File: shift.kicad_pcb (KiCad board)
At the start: 2 copper layers, 24 parts, among them P1 5v, P2 5v, P3 15Vpower-fixme, P4 digiin, P5 digicascade, P6 analog, P7 analog, P8 out, U1 74HC595, U2 TL074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

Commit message: updates... added correct header
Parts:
- added C5: 100n, Capacitors_ThroughHole:C_Rect_L7_W4.5_P5, F.Cu at (26.7, 50.5)
- added C6: 10uF, Discret:CP20, F.Cu at (110.2, 43.9)
- added C7: 10uF, Discret:CP20, F.Cu at (109.7, 71.6)
- added C8: 100n, Capacitors_ThroughHole:C_Rect_L7_W4.5_P5, F.Cu at (25.7, 32.8)
- added C9: 100n, Capacitors_ThroughHole:C_Rect_L7_W4.5_P5, F.Cu at (28.7, 20.1)
- added R3: bead, Resistors_ThroughHole:Resistor_Vertical_RM5mm, F.Cu at (59.7, 49.5)
- P3: value 15Vpower-fixme -> MTA-156-4; footprint Pin_Headers:Pin_Header_Straight_1x04 -> mta-156:MTA-156-4
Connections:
- P1 pad 1: 5v -> Net-(P1-Pad1)
- P1 pad 2: Net-(P1-Pad2) -> GND
- P2 pad 2: Net-(P1-Pad2) -> GND
- U1 pad 13: Net-(P1-Pad2) -> GND
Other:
- board text added: "+"
- board text added: "-"

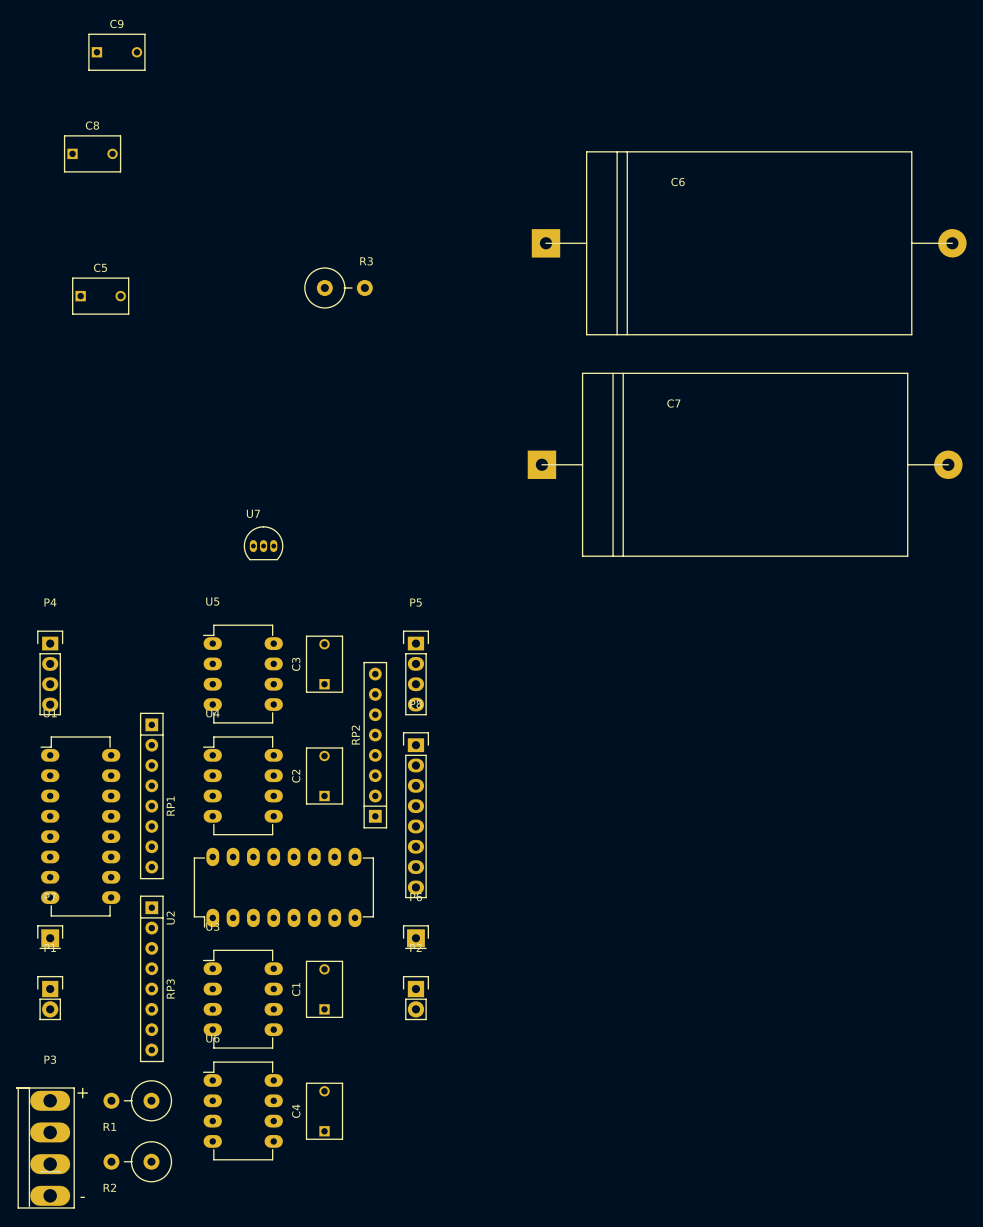
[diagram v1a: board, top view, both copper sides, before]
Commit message: decouple caps, all layed out [i think] except routing
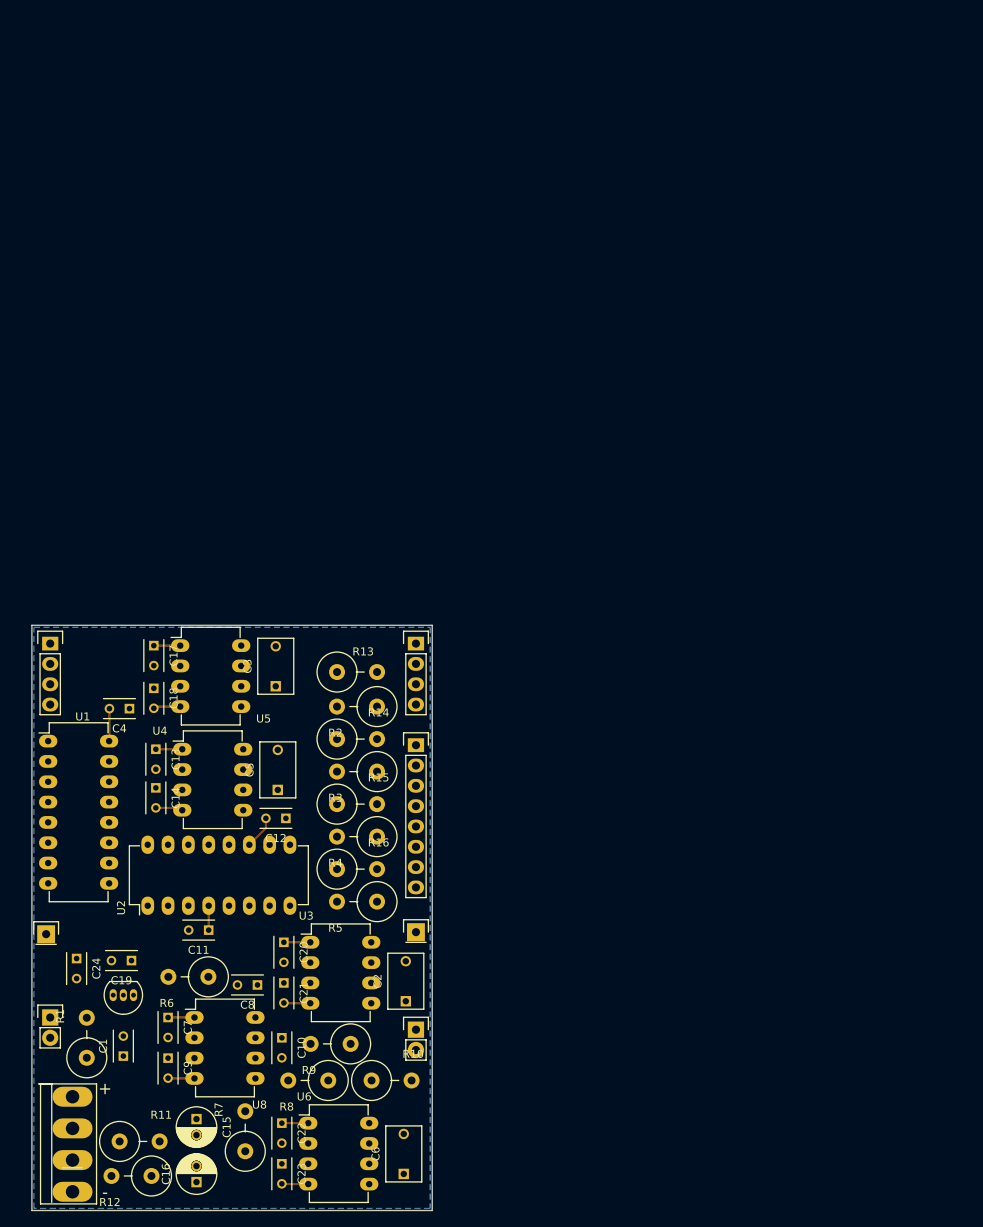
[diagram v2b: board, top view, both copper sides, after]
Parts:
- removed RP1, RP3: R_PACK4, Resistors_ThroughHole:Resistor_Array_SIP8
- removed RP2: 1k, Resistors_ThroughHole:Resistor_Array_SIP8
- added C10: 100pF, Capacitors_ThroughHole:C_Rect_L4_W2.5_P2.5, F.Cu at (51.8, 143.3)
- added C11: 100n, Capacitors_ThroughHole:C_Rect_L4_W2.5_P2.5, F.Cu at (42.7, 129.8)
- added C12: 100n, Capacitors_ThroughHole:C_Rect_L4_W2.5_P2.5, F.Cu at (52.3, 115.8)
- added C13: 10n, Capacitors_ThroughHole:C_Rect_L4_W2.5_P2.5, F.Cu at (36.1, 107.2)
- added C14: 10n, Capacitors_ThroughHole:C_Rect_L4_W2.5_P2.5, F.Cu at (36.1, 112.0)
- added C15: 10uF, Capacitors_ThroughHole:C_Radial_D5_L11_P2, F.Cu at (41.1, 153.4)
- added C16: 10uF, Capacitors_ThroughHole:C_Radial_D5_L11_P2, F.Cu at (41.1, 161.3)
- added C17: 10n, Capacitors_ThroughHole:C_Rect_L4_W2.5_P2.5, F.Cu at (35.8, 94.2)
- added C18: 10n, Capacitors_ThroughHole:C_Rect_L4_W2.5_P2.5, F.Cu at (35.8, 99.6)
- added C19: 100n, Capacitors_ThroughHole:C_Rect_L4_W2.5_P2.5, F.Cu at (33.0, 133.6)
- added C20: 10n, Capacitors_ThroughHole:C_Rect_L4_W2.5_P2.5, F.Cu at (52.1, 131.3)
- added C21: 10n, Capacitors_ThroughHole:C_Rect_L4_W2.5_P2.5, F.Cu at (52.1, 136.4)
- added C22: 10n, Capacitors_ThroughHole:C_Rect_L4_W2.5_P2.5, F.Cu at (51.8, 153.9)
- added C23: 10n, Capacitors_ThroughHole:C_Rect_L4_W2.5_P2.5, F.Cu at (51.8, 159.0)
- added C24: 100n, Capacitors_ThroughHole:C_Rect_L4_W2.5_P2.5, F.Cu at (26.2, 133.3)
- added R10: 220R, Resistors_ThroughHole:Resistor_Vertical_RM5mm, F.Cu at (65.5, 148.6)
- added R11: bead, Resistors_ThroughHole:Resistor_Vertical_RM5mm, F.Cu at (34.0, 156.2)
- added R12: bead, Resistors_ThroughHole:Resistor_Vertical_RM5mm, F.Cu at (33.0, 160.5)
- added R13: 1k, Resistors_ThroughHole:Resistor_Vertical_RM5mm, F.Cu at (61.2, 97.5)
- added R14: 1k, Resistors_ThroughHole:Resistor_Vertical_RM5mm, F.Cu at (61.2, 105.9)
- added R15: 1k, Resistors_ThroughHole:Resistor_Vertical_RM5mm, F.Cu at (61.2, 114.0)
- added R16: 1k, Resistors_ThroughHole:Resistor_Vertical_RM5mm, F.Cu at (61.2, 122.2)
- added R4: 1k, Resistors_ThroughHole:Resistor_Vertical_RM5mm, F.Cu at (61.2, 118.1)
- added R5: 1k, Resistors_ThroughHole:Resistor_Vertical_RM5mm, F.Cu at (61.2, 126.2)
- added R6: 4.7k, Resistors_ThroughHole:Resistor_Vertical_RM5mm, F.Cu at (40.1, 135.6)
- added R7: 220R, Resistors_ThroughHole:Resistor_Vertical_RM5mm, F.Cu at (47.2, 154.9)
- added R8: 1k, Resistors_ThroughHole:Resistor_Vertical_RM5mm, F.Cu at (55.1, 148.6)
- added R9: 4.7k, Resistors_ThroughHole:Resistor_Vertical_RM5mm, F.Cu at (57.9, 144.0)
- added U8: TL072, Housings_DIP:DIP-8_W7.62mm_LongPads, F.Cu at (40.9, 140.7)
- C1, C4: value C -> 100n; footprint Capacitors_ThroughHole:C_Rect_L7_W4.5_P5 -> Capacitors_ThroughHole:C_Rect_L4_W2.5_P2.5
- C5: value 100n -> C
- C6: value 10uF -> C; footprint Discret:CP20 -> Capacitors_ThroughHole:C_Rect_L7_W4.5_P5
- C7: value 10uF -> 100pF; footprint Discret:CP20 -> Capacitors_ThroughHole:C_Rect_L4_W2.5_P2.5
- C8, C9: footprint Capacitors_ThroughHole:C_Rect_L7_W4.5_P5 -> Capacitors_ThroughHole:C_Rect_L4_W2.5_P2.5
- P6: value analog -> ain
- P7: value analog -> aout
- R2, R3: value bead -> 1k
- moved C9 126.0 mm to (37.6, 145.8), turned to 270 degrees
- moved C6 124.1 mm to (67.1, 160.3), turned to 90 degrees
- moved C8 106.4 mm to (48.8, 136.7), turned to 180 degrees
- moved C7 99.9 mm to (37.6, 140.7), turned to 270 degrees
- moved C5 66.5 mm to (51.3, 112.3), turned to 90 degrees
- moved R2 63.5 mm to (61.2, 101.9)
- moved R3 60.5 mm to (61.2, 110.0), turned to 180 degrees
- moved C4 58.2 mm to (32.8, 102.1), turned to 180 degrees
- moved U7 58.1 mm to (33.3, 137.9), turned to 180 degrees
- moved P6 46.2 mm to (22.4, 130.3)
- moved P7 45.7 mm to (68.6, 130.0)
- moved C2 27.6 mm to (67.3, 138.7)
- moved C1 25.8 mm to (32.0, 145.5)
- moved U6 13.1 mm to (55.1, 153.9)
- moved U3 12.6 mm to (55.4, 131.3)
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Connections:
- C1 pad 1: Net-(C1-Pad1) -> 5v
- C4 pad 1: Net-(C4-Pad1) -> GND
- C4 pad 2: GND -> 5v
- C5 pad 1: 5v -> Net-(C5-Pad1)
- C6 pad 1: (no net) -> Net-(C6-Pad1)
- C7 pad 1: (no net) -> Net-(C7-Pad1)
- C7 pad 2: GND -> Net-(C7-Pad2)
- C9 pad 1: 5v -> GND
- C9 pad 2: GND -> -15V
- P6 pad 1: analogin -> Net-(P6-Pad1)
- P7 pad 1: analogin -> Net-(P7-Pad1)
- R1 pad 1: +15V -> 5v
- R1 pad 2: Net-(P3-Pad1) -> Net-(P1-Pad1)
- R2 pad 1: -15V -> dout0
- R2 pad 2: Net-(P3-Pad4) -> Net-(R2-Pad2)
- R3 pad 1: 5v -> dout1
- R3 pad 2: Net-(P1-Pad1) -> Net-(R3-Pad2)
- U1 pad 1: Net-(RP3-Pad1) -> Net-(R2-Pad2)
- U1 pad 15: Net-(RP1-Pad1) -> trig0
- U1 pad 2: Net-(RP1-Pad2) -> trig1
- U1 pad 3: Net-(RP3-Pad2) -> Net-(R3-Pad2)
- U1 pad 4: Net-(RP1-Pad3) -> trig2
- U1 pad 6: Net-(RP1-Pad4) -> trig3
- U2 pad 10: aout2 -> aout1
- U2 pad 5: aout1 -> aout2
- U2 pad 7: aout1 -> aout2
- U2 pad 8: aout2 -> aout1
- U3 pad 6: Net-(C1-Pad1) -> Net-(C2-Pad1)
- U4 pad 5: Net-(U2-Pad6) -> Net-(U2-Pad9)
- U4 pad 6: Net-(C2-Pad1) -> Net-(C5-Pad1)
- U5 pad 5: Net-(U2-Pad9) -> Net-(U2-Pad6)
- U6 pad 6: Net-(C4-Pad1) -> Net-(C6-Pad1)
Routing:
- net -15V: track 0.00 -> 20.9 mm
- net +15V: track 0.00 -> 16.3 mm
- net 5v: track 0.00 -> 4.08 mm
- net Net-(C7-Pad1): track 0.00 -> 3.30 mm
- added copper zone on B.Cu, net GND
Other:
- board outline added: 50 x 73.2 mm

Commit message: auto routed and filled
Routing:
- net +15V: track 16.3 -> 118.5 mm
- net 5v: track 4.08 -> 98.3 mm
- net -15V: track 20.9 -> 111.2 mm
- net Net-(P5-Pad1): track 0.00 -> 81.9 mm
- net analogin: track 0.00 -> 78.9 mm
- net Net-(P4-Pad2): track 0.00 -> 77.1 mm
- net Net-(P4-Pad4): track 0.00 -> 74.1 mm
- net aout0: track 0.00 -> 72.6 mm
- net Net-(P4-Pad3): track 0.00 -> 70.6 mm
- net trig3: track 0.00 -> 69.0 mm
- net Net-(U2-Pad13): track 0.00 -> 52.5 mm
- net trig0: track 0.00 -> 44.9 mm, vias 0 -> 1
- net Net-(R3-Pad2): track 0.00 -> 40.9 mm
- net Net-(R4-Pad2): track 0.00 -> 40.6 mm
- net Net-(R5-Pad2): track 0.00 -> 38.8 mm
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
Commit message: everything is hooked up, moved around too
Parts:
- C10, C7: value 100pF -> 100p
- C2, C3, C5, C6: value C -> 100n
- moved C10 0.51 mm to (51.8, 143.8)
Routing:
- net GND: track 0.00 -> 99.7 mm, vias 0 -> 12
- net Net-(P5-Pad1): track 81.9 -> 63.9 mm
- net aout0: track 72.6 -> 58.1 mm
- net Net-(P4-Pad2): track 77.1 -> 86.7 mm
- net trig1: track 26.1 -> 19.6 mm
- net trig0: track 44.9 -> 50.7 mm
- net analogin: track 78.9 -> 73.7 mm
- net Net-(P4-Pad1): track 25.4 -> 21.0 mm
- net 5v: track 98.3 -> 94.2 mm
- net -15V: track 111.2 -> 114.9 mm, vias 0 -> 2
- net Net-(R3-Pad2): track 40.9 -> 44.4 mm
- net Net-(P4-Pad3): track 70.6 -> 67.4 mm
- net Net-(P4-Pad4): track 74.1 -> 71.0 mm
- net Net-(U2-Pad2): track 31.4 -> 34.3 mm
- net Net-(R6-Pad1): track 24.5 -> 27.4 mm
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
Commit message: added some text
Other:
- board text added: "XNOR 10/16"
- board text added: "shift+samp/hold"
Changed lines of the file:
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@@
     (area 20.376999 87.905 70.687001 164.921001)
     (thickness 1.6)
-    (drawings 6)
+    (drawings 8)
     (tracks 506)
     (zones 0)
@@
       (net 34 5v))
   )
+  (gr_text shift+samp/hold (at 45.212 122.682) (layer B.SilkS)
+    (effects (font (size 1.5 1.5) (thickness 0.3)) (justify mirror))
+  )
+  (gr_text "XNOR\n10/16" (at 29.464 95.6945) (layer B.SilkS)
+    (effects (font (size 1.5 1.5) (thickness 0.3)) (justify mirror))
+  )
   (gr_line (start 70.612 164.846) (end 70.612 91.694) (angle 90) (layer Edge.Cuts) (width 0.15))

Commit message: updated with new footprints, need to layout
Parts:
- C15, C16: footprint Capacitors_ThroughHole:C_Radial_D5_L11_P2 -> Capacitors_ThroughHole:CP_Radial_Tantal_D7.0mm_P2.50mm
- U2: footprint Housings_DIP:DIP-16_W7.62mm_LongPads -> Housings_DIP:DIP-14_W7.62mm_Socket_LongPads
- U7: footprint TO_SOT_Packages_THT:TO-92_Inline_Narrow_Oval -> TO_SOT_Packages_THT:TO-220_Vertical
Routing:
- net Net-(U2-Pad13): track 52.3 -> 1.13 mm
- net -15V: track 114.9 -> 155.1 mm
- net GND: track 99.7 -> 117.1 mm
- net 5v: track 94.2 -> 76.8 mm
- net aout1: track 28.1 -> 44.8 mm
- net aout3: track 22.9 -> 6.19 mm
- net Net-(U2-Pad9): track 8.62 -> 19.6 mm
